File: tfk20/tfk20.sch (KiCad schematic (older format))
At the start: 33 parts, among them J1 USB_C_Receptacle_USB2.0, J2 Conn_01x06_Male, Q1 DTC123J, SW1 Reset, U1 MCP1700-3302E_SOT23, U2 USBLC6-2SC6, U3 STM32F072CBTx

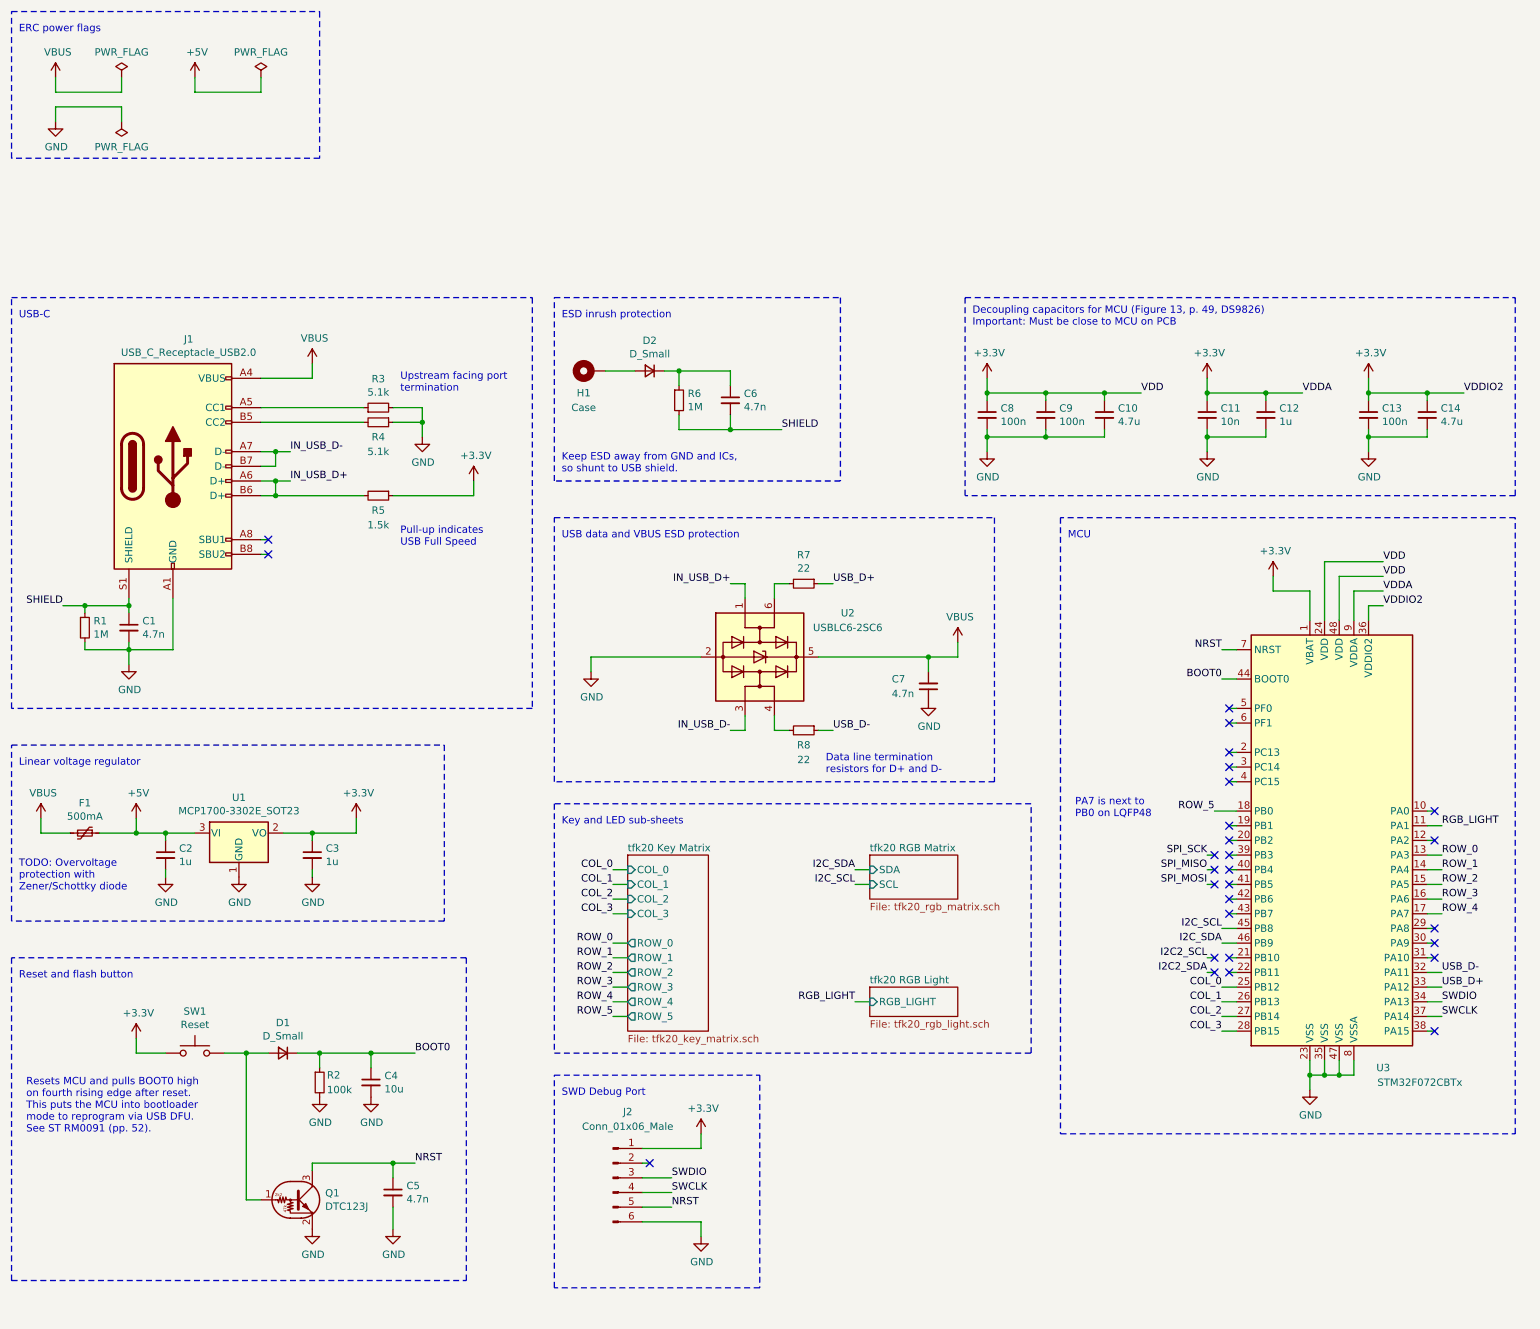
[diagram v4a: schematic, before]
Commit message: Implement sophisticated USB-C protection
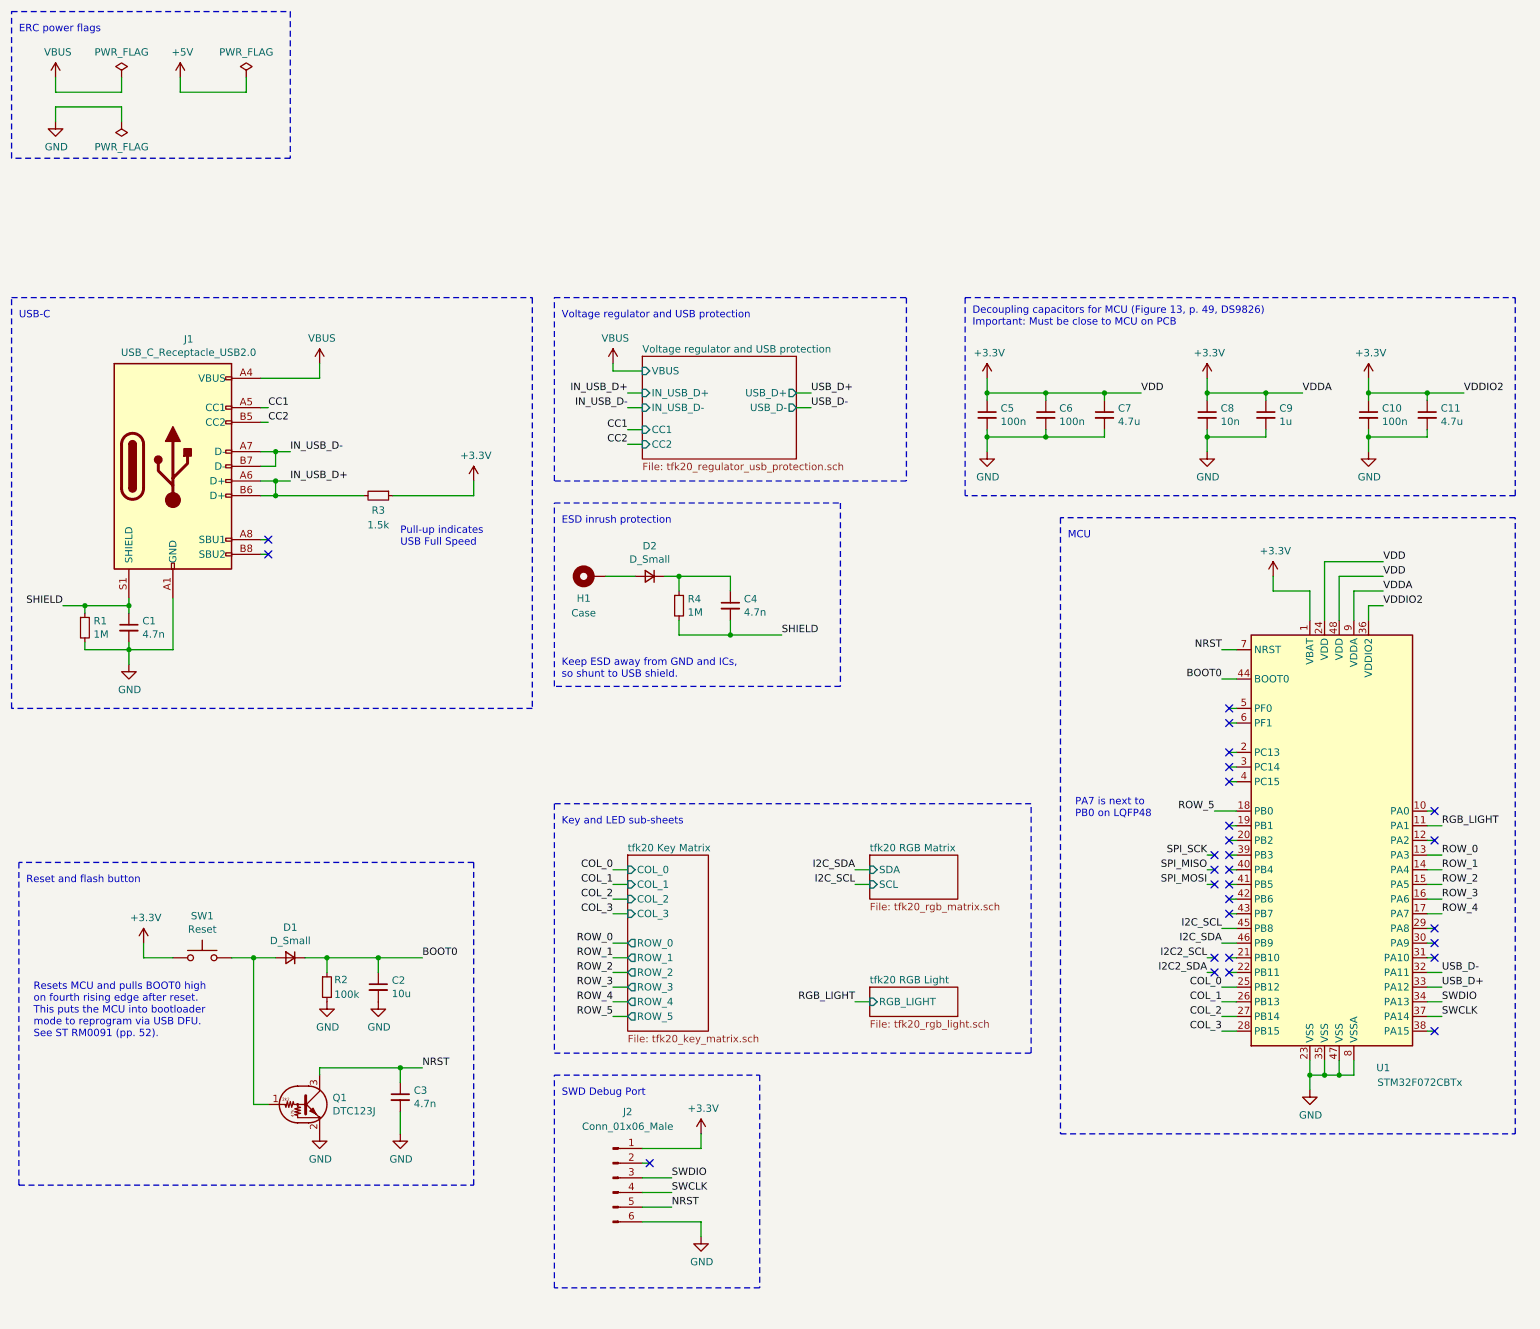
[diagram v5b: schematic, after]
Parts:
- removed C2, C3: 1u, symbol Device:C_Small
- removed C6, C7: 4.7n, symbol Device:C_Small
- removed F1: 500mA, symbol Device:Polyfuse_Small
- removed R3: 5.1k, symbol Device:R_Small
- removed R6: 1M, symbol Device:R_Small
- removed R7, R8: 22, symbol Device:R_Small
- removed U1: MCP1700-3302E_SOT23, Package_TO_SOT_SMD:SOT-23, symbol Regulator_Linear:MCP1700-3302E_SOT23
- removed U2: USBLC6-2SC6, Package_TO_SOT_SMD:SOT-23-6, symbol Power_Protection:USBLC6-2SC6
- added C4: 4.7n, symbol Device:C_Small
- R4: value 5.1k -> 1M
- renumbered C13 to C10, C14 to C11, C4 to C2, C5 to C3, C8 to C5, C9 to C6, C10 to C7, C11 to C8, C12 to C9, R5 to R3, U3 to U1
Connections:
- net GND: no longer R4.1
- net SHIELD: now also R4.2, C4.2
- net CC1: now reaches J1.A5 (CC1)
- net CC2: now reaches J1.B5 (CC2)
- net CC2: no longer R4.2
- net at D2.1 (K): now also R4.1, C4.1
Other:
- note added: "Voltage regulator and USB protection"
- note removed: "Data line termination \nresistors for D+ and D-"
- note removed: "Linear voltage regulator"
- note removed: "TODO: Overvoltage \nprotection with \nZener/Schottky diode"
- note removed: "USB data and VBUS ESD protection"
- note removed: "Upstream facing port \ntermination"
- moved on the sheet: C2, C3, D1, Q1, R2, SW1

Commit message: Add STL11N3LLH6 footprint
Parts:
- renumbered C1 to C101, C2 to C102, C3 to C103, C4 to C104, C5 to C105, C6 to C106, C7 to C107, C8 to C108, C9 to C109, C10 to C110, C11 to C111, D1 to D101, D2 to D102, H1 to H101, J1 to J101, J2 to J102, Q1 to Q101, R1 to R101, R2 to R102, R3 to R103, R4 to R104, SW1 to SW101, U1 to U101
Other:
- moved on the sheet: R103

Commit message: Fix project
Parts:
- renumbered R103 to R102, R102 to R103
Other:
- note added: "See https://acheronproject.com/\nreset_article/principle.html for more\ninformation about this circuit.\n"
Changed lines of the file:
@@
 Connection ~ 2500 2050
 $Comp
-L power:+3.3V #PWR0111
+L power:+3.3V #PWR0110
 U 1 1 602BB638
 P 3350 1950
-F 0 "#PWR0111" H 3350 1800 50  0001 C CNN
+F 0 "#PWR0110" H 3350 1800 50  0001 C CNN
 F 1 "+3.3V" H 3365 2123 50  0000 C CNN
 F 2 "" H 3350 1950 50  0001 C CNN
@@
 $EndComp
 $Comp
-L Device:R_Small R103
+L Device:R_Small R102
 U 1 1 602BC2DD
 P 2800 2050
-F 0 "R103" V 2900 2050 50  0000 C CNN
+F 0 "R102" V 2900 2050 50  0000 C CNN
 F 1 "1.5k" V 3000 2050 50  0000 C CNN
 F 2 "" H 2800 2050 50  0001 C CNN
@@
 	3350 6400 3350 6250
 $Comp
-L power:GND #PWR0110
+L power:GND #PWR0111
 U 1 1 60342BE5
 P 3350 6400
-F 0 "#PWR0110" H 3350 6150 50  0001 C CNN
+F 0 "#PWR0111" H 3350 6150 50  0001 C CNN
 F 1 "GND" H 3355 6227 50  0000 C CNN
 F 2 "" H 3350 6400 50  0001 C CNN
@@
 $EndComp
 $Comp
-L power:GND #PWR0107
+L power:GND #PWR0106
 U 1 1 6033851F
 P 2800 6400
-F 0 "#PWR0107" H 2800 6150 50  0001 C CNN
+F 0 "#PWR0106" H 2800 6150 50  0001 C CNN
 F 1 "GND" H 2805 6227 50  0000 C CNN
 F 2 "" H 2800 6400 50  0001 C CNN
@@
 $EndComp
 $Comp
-L power:GND #PWR0109
+L power:GND #PWR0108
 U 1 1 60318D15
 P 3200 5500
-F 0 "#PWR0109" H 3200 5250 50  0001 C CNN
+F 0 "#PWR0108" H 3200 5250 50  0001 C CNN
 F 1 "GND" H 3205 5327 50  0000 C CNN
 F 2 "" H 3200 5500 50  0001 C CNN
@@
 $EndComp
 $Comp
-L power:GND #PWR0108
+L power:GND #PWR0107
 U 1 1 60318948
 P 2850 5500
-F 0 "#PWR0108" H 2850 5250 50  0001 C CNN
+F 0 "#PWR0107" H 2850 5250 50  0001 C CNN
 F 1 "GND" H 2855 5327 50  0000 C CNN
 F 2 "" H 2850 5500 50  0001 C CNN
@@
 $EndComp
 $Comp
-L Device:R_Small R102
+L Device:R_Small R103
 U 1 1 602D61C3
 P 2850 5400
-F 0 "R102" H 2900 5450 50  0000 L CNN
+F 0 "R103" H 2900 5450 50  0000 L CNN
 F 1 "100k" H 2900 5350 50  0000 L CNN
 F 2 "" H 2850 5400 50  0001 C CNN
@@
 	2400 1250 3350 1250
 $Comp
-L power:VBUS #PWR0106
+L power:VBUS #PWR0109
 U 1 1 60A3DDCB
 P 3350 1150
-F 0 "#PWR0106" H 3350 1000 50  0001 C CNN
+F 0 "#PWR0109" H 3350 1000 50  0001 C CNN
 F 1 "VBUS" H 3365 1323 50  0000 C CNN
 F 2 "" H 3350 1150 50  0001 C CNN
@@
 	1    0    0    -1
 $EndComp
+Text Notes 850  6100 0    50   ~ 0
+See https://acheronproject.com/\nreset_article/principle.html for more\ninformation about this circuit.\n
 $EndSCHEMATC
